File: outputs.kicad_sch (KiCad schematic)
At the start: 48 parts, among them J10 Screw_Terminal_01x02, J3 Screw_Terminal_01x03, J4 Screw_Terminal_01x03, J5 Screw_Terminal_01x02, J6 Screw_Terminal_01x02, J7 Screw_Terminal_01x02, J8 Screw_Terminal_01x02, J9 Screw_Terminal_01x02, Q1 IRLZ44N, Q2 IRLZ44N, Q3 IRLZ44N, Q4 IRLZ44N, Q5 IRLZ44N, Q6 IRLZ44N, U2 74AHCT125, U3 74AHCT125

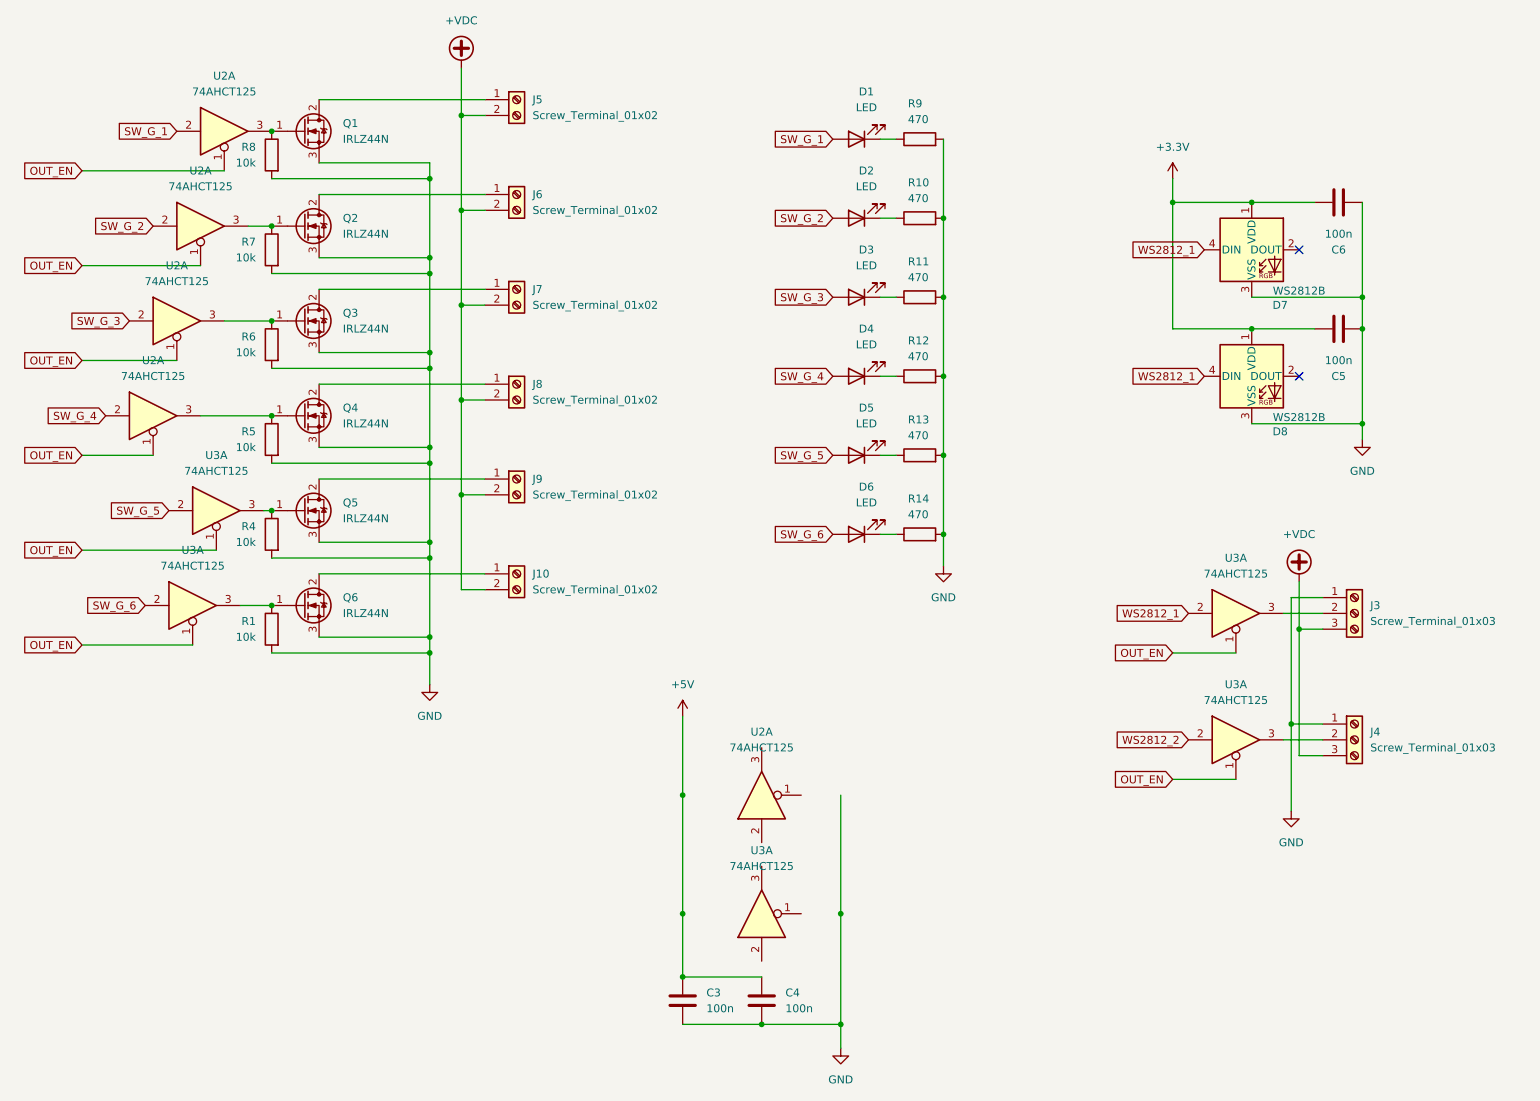
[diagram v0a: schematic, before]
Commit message: mcu pinouts and extras
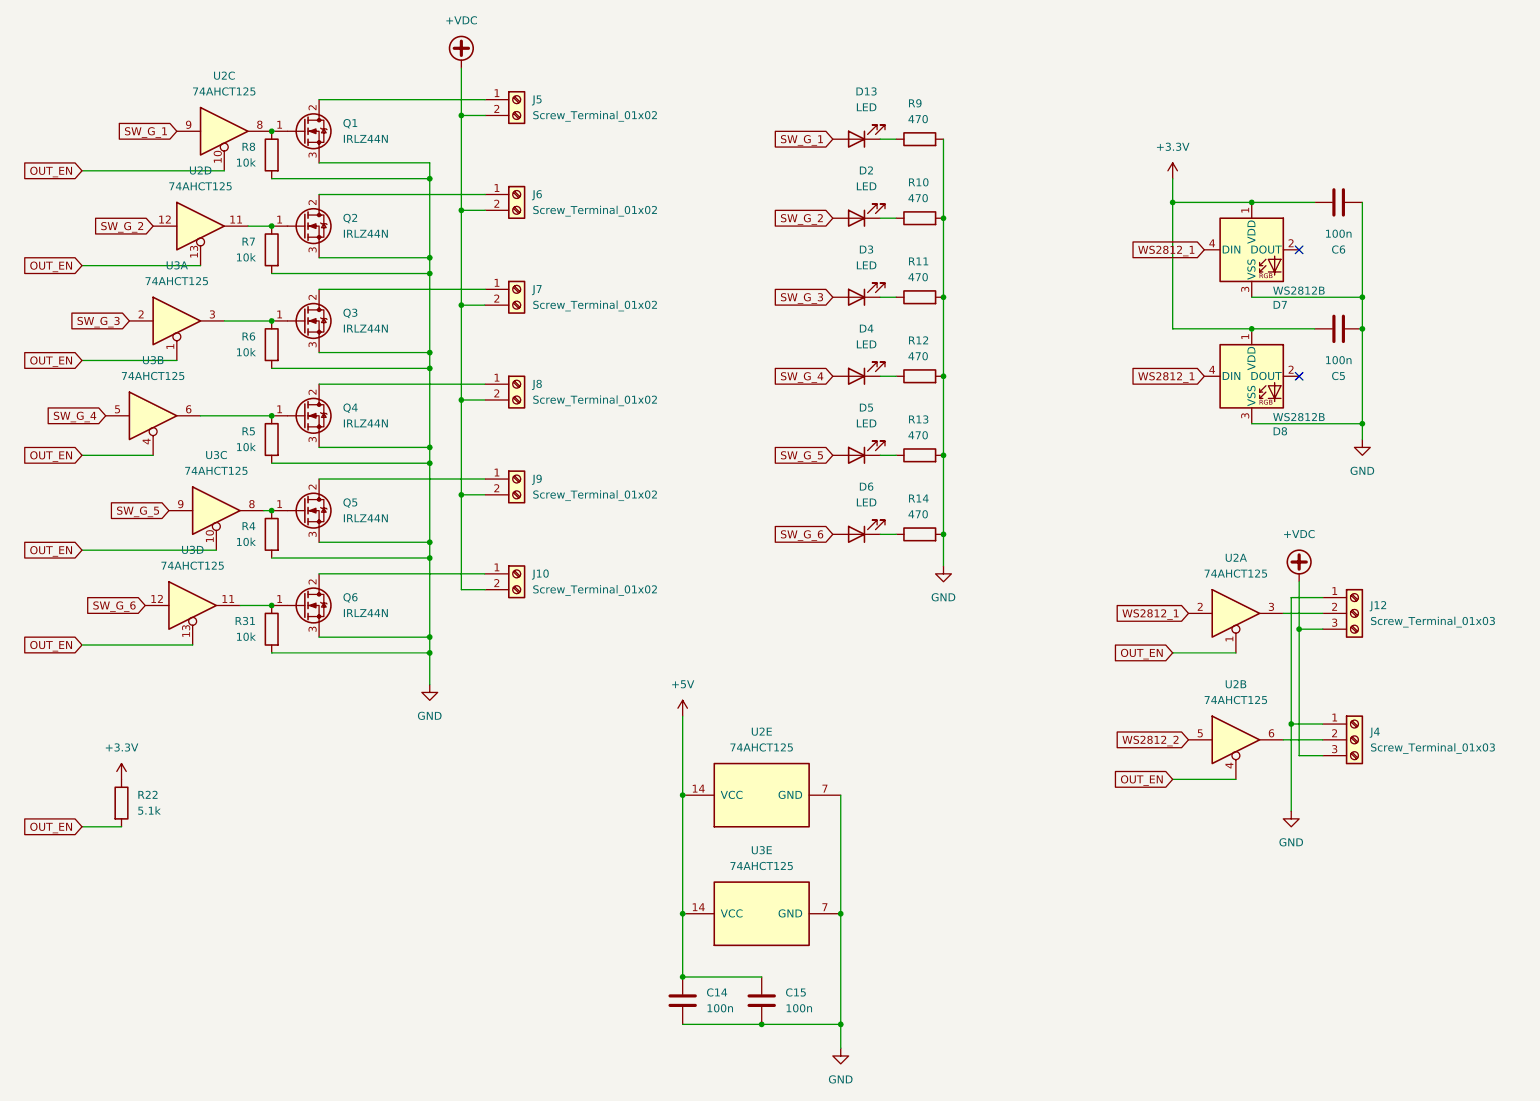
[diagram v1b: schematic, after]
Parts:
- removed U2 (x5): 74AHCT125, Package_SO:SOIC-14_3.9x8.7mm_P1.27mm, symbol 74xx:74AHCT125
- removed U3 (x5): 74AHCT125, symbol 74xx:74AHCT125
- added R22: 5.1k, Resistor_SMD:R_0603_1608Metric_Pad0.98x0.95mm_HandSolder, symbol Device:R
- added U2, U3: 74AHCT125, Package_SO:SOIC-14_3.9x8.7mm_P1.27mm, symbol 74xx:74AHCT125
- renumbered C3 to C14, C4 to C15, D1 to D13, J3 to J12, R1 to R31
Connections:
- net +3.3V: now also R22.1
- net +5V: now also U2.14 (VCC), U3.14 (VCC)
- net GND: now also U2.7 (GND), U3.7 (GND)
- net OUT_EN: now also R22.2, U2.1, U2.10, U2.13, U2.4, U3.1, U3.10, U3.13, U3.4
- net SW_G_1: now also U2.9
- net SW_G_2: now also U2.12
- net SW_G_3: now also U3.2
- net SW_G_4: now also U3.5
- net SW_G_5: now also U3.9
- net SW_G_6: now also U3.12
- net WS2812_1: now also U2.2
- net WS2812_2: now also U2.5
- net at Q1.1 (G), R8.1: now also U2.8
- net at J12.2 (Pin_2): now also U2.3
- net at Q2.1 (G), R7.1: now also U2.11
- net at Q4.1 (G), R5.1: now also U3.6
- net at Q5.1 (G), R4.1: now also U3.8
- net at J4.2 (Pin_2): now also U2.6
- net at Q6.1 (G), R31.1: now also U3.11
- net at Q3.1 (G), R6.1: now also U3.3

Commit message: add probe headers
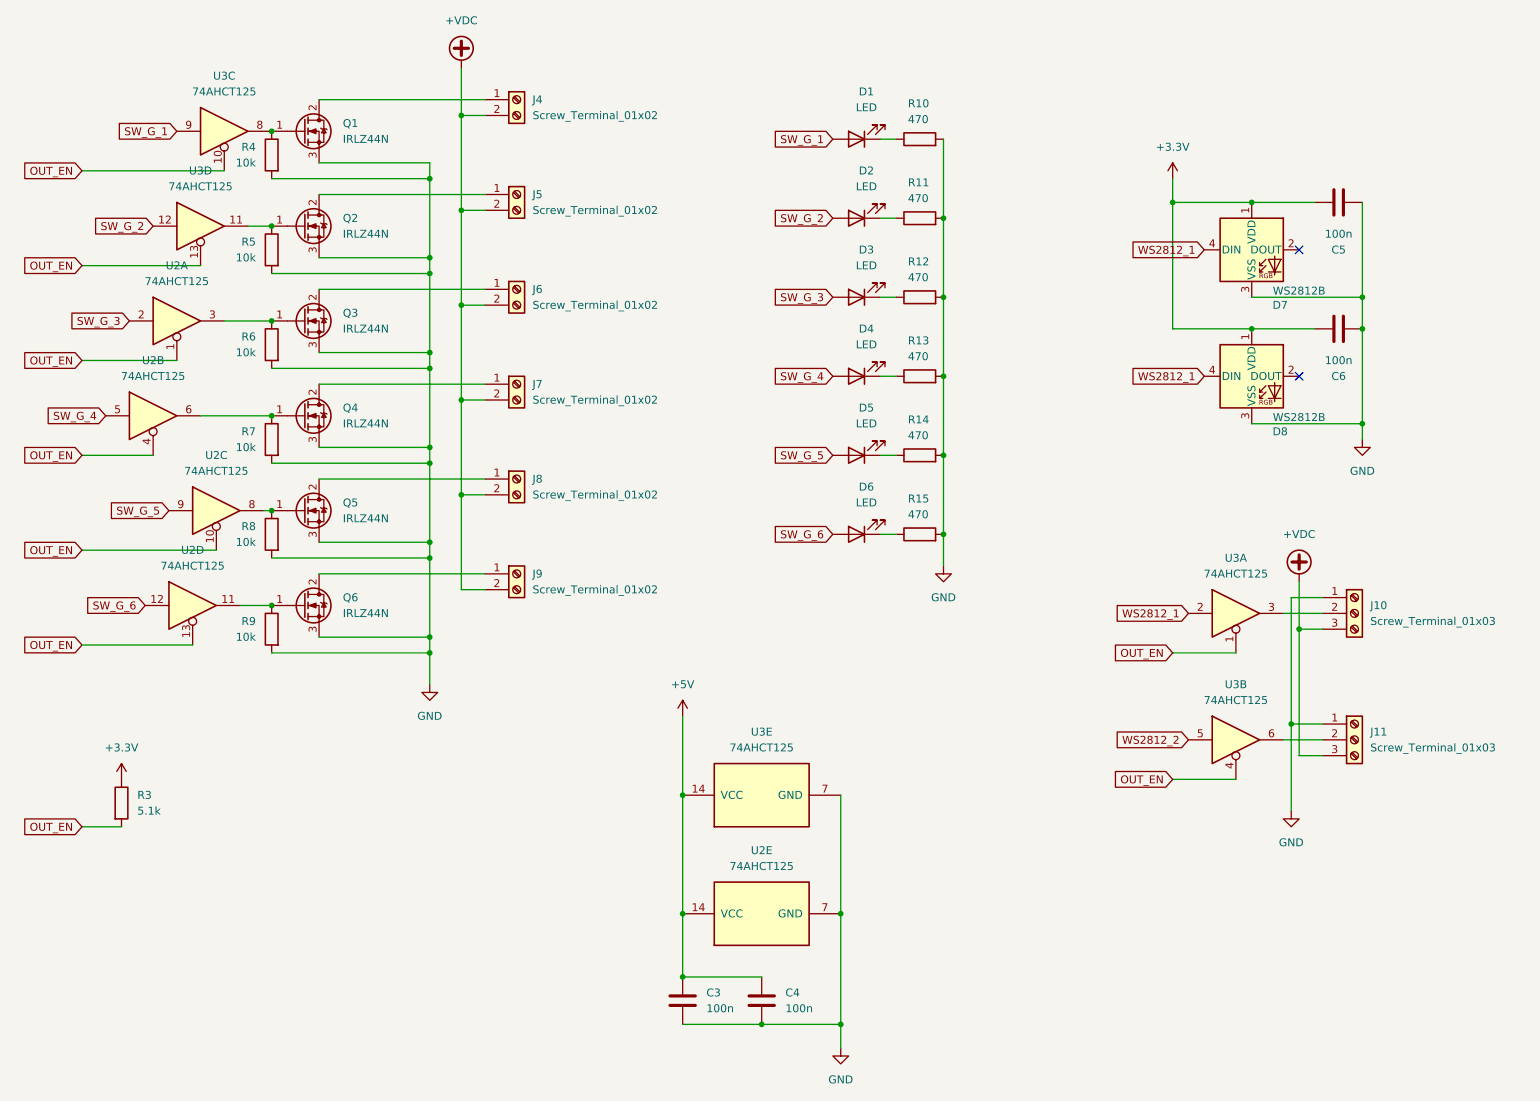
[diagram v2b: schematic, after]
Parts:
- renumbered C14 to C3, C15 to C4, C6 to C5, C5 to C6, D13 to D1, J12 to J10, J4 to J11, J5 to J4, J6 to J5, J7 to J6, J8 to J7, J9 to J8, J10 to J9, R9 to R10, R10 to R11, R11 to R12, R12 to R13, R13 to R14, R14 to R15, R22 to R3, R8 to R4, R7 to R5, R5 to R7, R4 to R8, R31 to R9, U3 to U2, U2 to U3

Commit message: partial layout
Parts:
- added J16: Conn_02x04_Top_Bottom, Connector_PinHeader_2.54mm:PinHeader_2x04_P2.54mm_Vertical, symbol Connector_Generic:Conn_02x04_Top_Bottom
- renumbered C3 to C5, C4 to C6, C5 to C7, C6 to C8, R9 to R10, R10 to R11, R11 to R12, R12 to R13, R13 to R14, R14 to R15, R15 to R16, R3 to R4, R4 to R5, R5 to R6, R6 to R7, R7 to R8, R8 to R9
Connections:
- net SW_G_1: now also J16.1 (Pin_1)
- net SW_G_2: now also J16.2 (Pin_2)
- net SW_G_3: now also J16.3 (Pin_3)
- net SW_G_4: now also J16.4 (Pin_4)
- net SW_G_5: now also J16.7 (Pin_7)
- net SW_G_6: now also J16.8 (Pin_8)
- net WS2812_1: now also J16.5 (Pin_5)
- net WS2812_2: now also J16.6 (Pin_6)

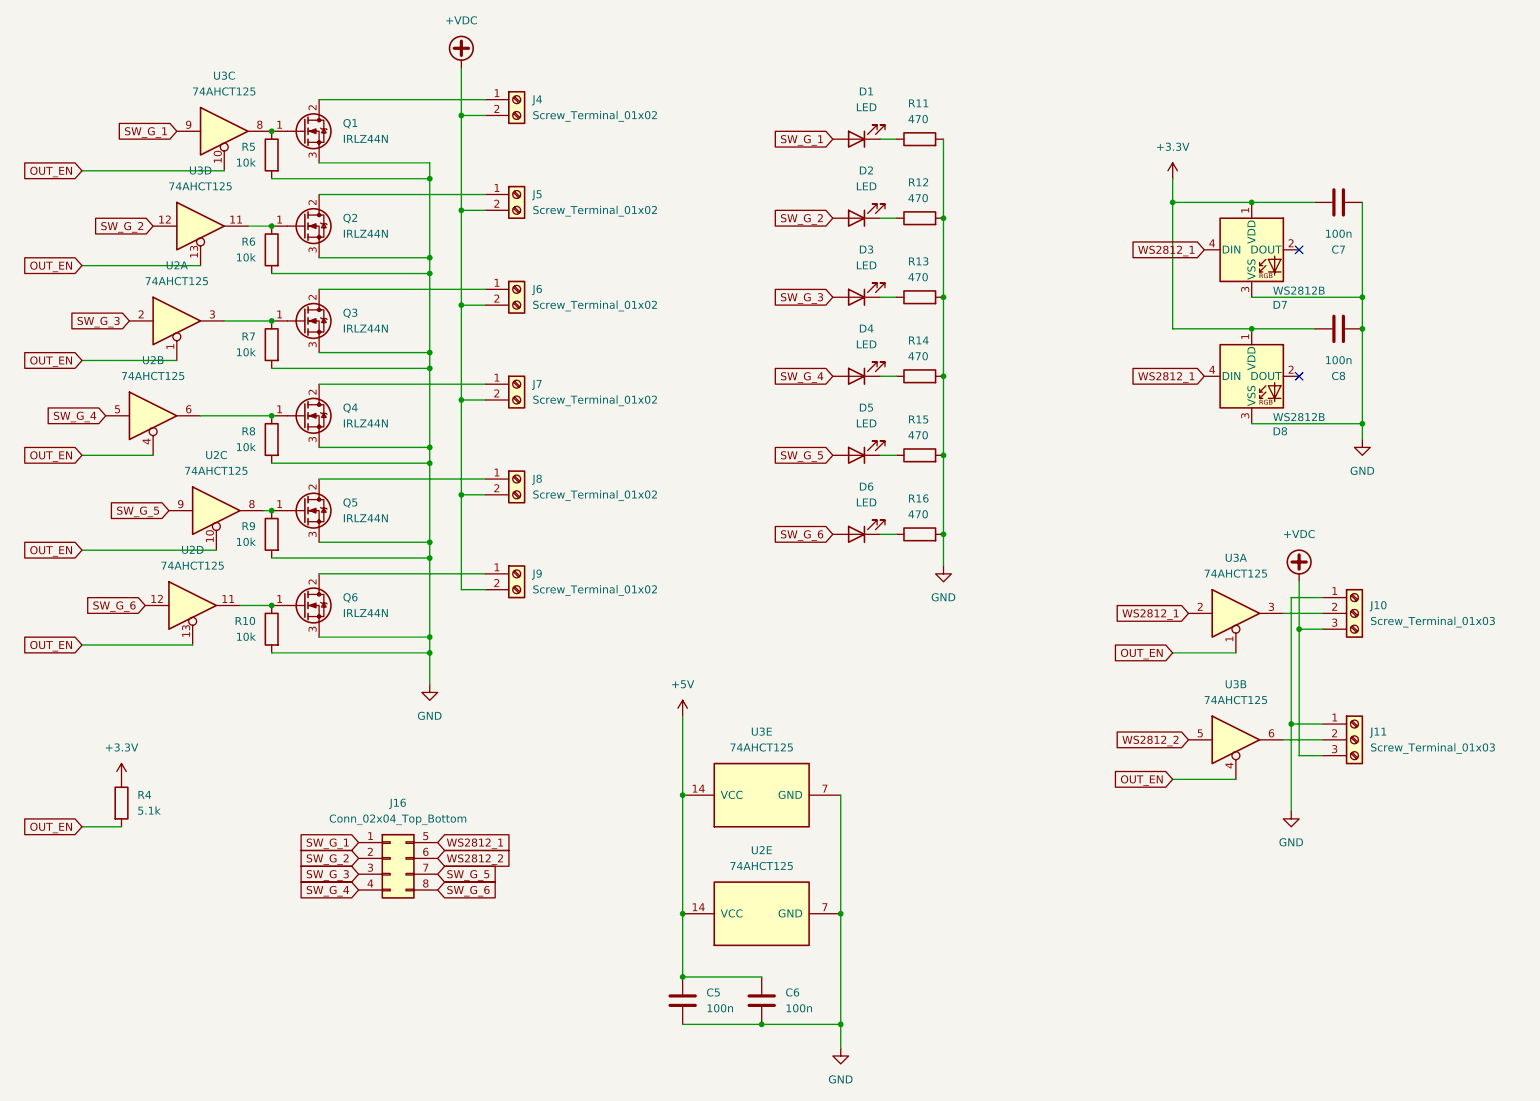
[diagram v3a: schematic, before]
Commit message: schematic changes for mini
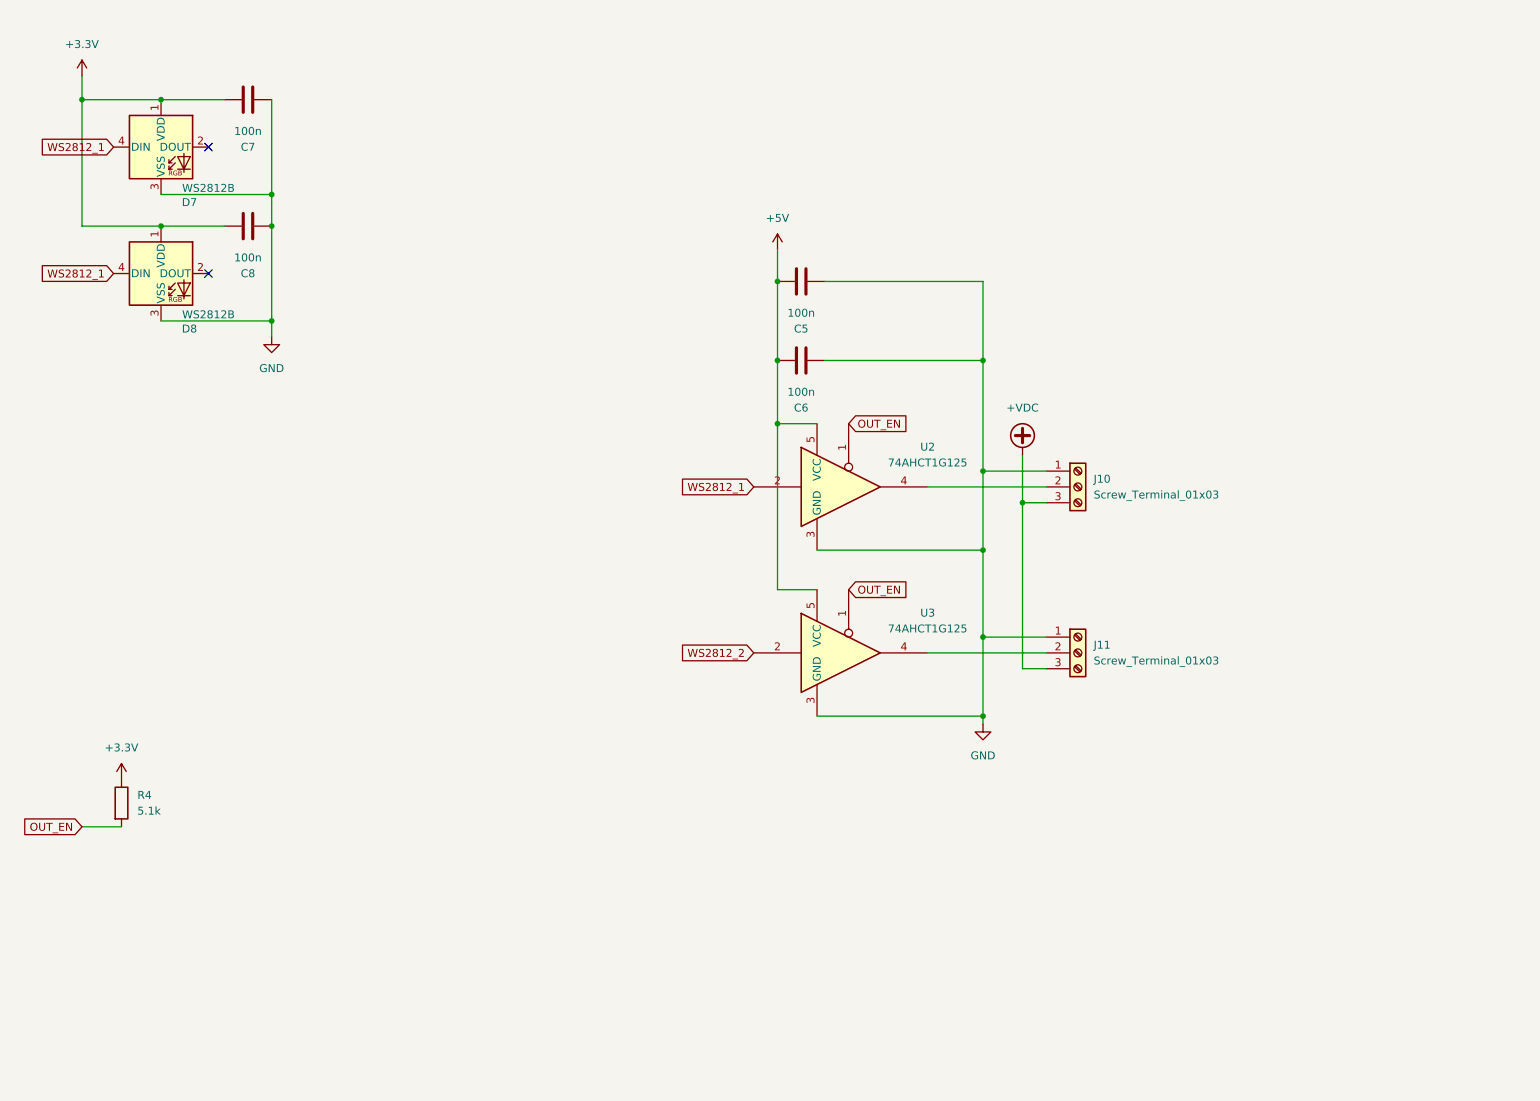
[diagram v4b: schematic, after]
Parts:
- removed D1, D2, D3, D4, D5, D6: LED, LED_SMD:LED_0603_1608Metric_Pad1.05x0.95mm_HandSolder, symbol Device:LED
- removed J16: Conn_02x04_Top_Bottom, Connector_PinHeader_2.54mm:PinHeader_2x04_P2.54mm_Vertical, symbol Connector_Generic:Conn_02x04_Top_Bottom
- removed J4, J5, J6, J7, J8, J9: Screw_Terminal_01x02, TerminalBlock_MetzConnect:TerminalBlock_MetzConnect_Type101_RT01602HBWC_1x02_P5.08mm_Horizontal, symbol Connector:Screw_Terminal_01x02
- removed Q1, Q2, Q3, Q4, Q5, Q6: IRLZ44N, Package_TO_SOT_THT:TO-220-3_Vertical, symbol Transistor_FET:IRLZ44N
- removed R10, R5, R6, R7, R8, R9: 10k, Resistor_SMD:R_0603_1608Metric_Pad0.98x0.95mm_HandSolder, symbol Device:R
- removed R11, R12, R13, R14, R15, R16: 470, Resistor_SMD:R_0603_1608Metric_Pad0.98x0.95mm_HandSolder, symbol Device:R
- removed U2, U3: 74AHCT125, Package_SO:SOIC-14_3.9x8.7mm_P1.27mm, symbol 74xx:74AHCT125
- added U2, U3: 74AHCT1G125, Package_TO_SOT_SMD:SOT-353_SC-70-5_Handsoldering, symbol 74xGxx:74AHCT1G125
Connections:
- net +5V: now also C5.1, C6.1, U2.5 (VCC), U3.5 (VCC); no longer C5.2, C6.2
- net GND: now also C5.2, C6.2, U2.3 (GND), U3.3 (GND); no longer C5.1, C6.1
- net OUT_EN: now also U2.1, U3.1
- net WS2812_1: now also U2.2
- net WS2812_2: now also U3.2
- net at J10.2 (Pin_2): now also U2.4
- net at J11.2 (Pin_2): now also U3.4
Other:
- moved on the sheet: C7, C8, D7, D8, J10, J11
